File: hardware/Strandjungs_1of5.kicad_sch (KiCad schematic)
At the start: 9 parts, among them J1 Screw_Terminal_01x02, J10 Conn_01x02, J11 Conn_01x02, J12 Conn_01x02, J7 Screw_Terminal_01x02, J8 Screw_Terminal_01x02, J9 Conn_01x02, SW1 SW_DIP_x02

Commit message: first iteration of layout almost done
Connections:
- net RESET: now also A1.9 (D6); no longer A1.8 (D5)
- net TRIGGER: now also A1.8 (D5); no longer A1.9 (D6)
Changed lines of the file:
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@@
     (stroke (width 0) (type default) (color 0 0 0 0))
   )
-  (wire (pts (xy 136.525 83.82) (xy 136.525 94.615))
-    (stroke (width 0) (type default) (color 0 0 0 0))
-  )
-  (wire (pts (xy 136.525 94.615) (xy 151.765 94.615))
+  (wire (pts (xy 137.16 94.615) (xy 151.765 94.615))
     (stroke (width 0) (type default) (color 0 0 0 0))
   )
@@
     (stroke (width 0) (type default) (color 0 0 0 0))
   )
-  (wire (pts (xy 111.76 86.36) (xy 133.985 86.36))
+  (wire (pts (xy 111.76 86.36) (xy 123.825 86.36))
     (stroke (width 0) (type default) (color 0 0 0 0))
   )
@@
   )
   (wire (pts (xy 231.775 34.925) (xy 247.65 34.925))
-    (stroke (width 0) (type default) (color 0 0 0 0))
-  )
-  (wire (pts (xy 133.985 86.36) (xy 133.985 105.41))
     (stroke (width 0) (type default) (color 0 0 0 0))
   )
@@
     (stroke (width 0) (type default) (color 0 0 0 0))
   )
-  (wire (pts (xy 133.985 105.41) (xy 151.765 105.41))
+  (wire (pts (xy 137.16 105.41) (xy 151.765 105.41))
     (stroke (width 0) (type default) (color 0 0 0 0))
   )
@@
     (stroke (width 0) (type default) (color 0 0 0 0))
   )
-  (wire (pts (xy 111.76 83.82) (xy 136.525 83.82))
+  (wire (pts (xy 111.76 83.82) (xy 123.825 83.82))
     (stroke (width 0) (type default) (color 0 0 0 0))
   )
@@
   )
   (label "SWITCH1" (at 233.045 34.925 0)
+    (effects (font (size 1.27 1.27)) (justify left bottom))
+  )
+  (label "TRIGGER" (at 113.0265 83.82 0)
     (effects (font (size 1.27 1.27)) (justify left bottom))
   )
@@
     (effects (font (size 1.27 1.27)) (justify left bottom))
   )
+  (label "RESET" (at 113.03 86.36 0)
+    (effects (font (size 1.27 1.27)) (justify left bottom))
+  )

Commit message: added 7805 as voltage regulator
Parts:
- added R16: dnp, Resistor_SMD:R_0603_1608Metric, symbol Device:R
- added U1: L7805, Package_TO_SOT_THT:TO-220-3_Vertical, symbol Regulator_Linear:L7805
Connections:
- net +12V: now also R16.1, U1.1 (IN)
- net GND: now also U1.2 (GND)
- net +5V: now reaches A1.27 (+5V)
- net +5V: now also U1.3 (OUT)
- net at A1.30 (VIN): now also R16.2
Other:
- note added: "alternative powering if regulator on Arduino supports this"
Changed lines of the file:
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@@
+    (stroke (width 0) (type default) (color 0 0 0 0))
+  )
+  (wire (pts (xy 65.405 53.34) (xy 65.405 54.61))
+    (stroke (width 0) (type default) (color 0 0 0 0))
+  )
+  (wire (pts (xy 101.6 50.8) (xy 101.6 52.07))
     (stroke (width 0) (type default) (color 0 0 0 0))
   )
@@
     (stroke (width 0) (type default) (color 0 0 0 0))
   )
+  (wire (pts (xy 73.025 45.72) (xy 75.565 45.72))
+    (stroke (width 0) (type default) (color 0 0 0 0))
+  )
   (bus (pts (xy 126.365 104.14) (xy 126.365 118.745))
     (stroke (width 0) (type default) (color 0 0 0 0))
@@
     (stroke (width 0) (type default) (color 0 0 0 0))
   )
+  (wire (pts (xy 75.565 45.72) (xy 75.565 43.815))
+    (stroke (width 0) (type default) (color 0 0 0 0))
+  )
   (wire (pts (xy 111.76 76.2) (xy 123.825 76.2))
     (stroke (width 0) (type default) (color 0 0 0 0))
@@
     (stroke (width 0) (type default) (color 0 0 0 0))
   )
+  (wire (pts (xy 93.98 58.42) (xy 93.98 60.96))
+    (stroke (width 0) (type default) (color 0 0 0 0))
+  )
   (bus (pts (xy 229.235 24.765) (xy 229.235 37.465))
     (stroke (width 0) (type default) (color 0 0 0 0))
@@
     (stroke (width 0) (type default) (color 0 0 0 0))
   )
+  (wire (pts (xy 57.785 45.72) (xy 56.515 45.72))
+    (stroke (width 0) (type default) (color 0 0 0 0))
+  )
   (bus (pts (xy 229.235 113.665) (xy 224.155 118.745))
     (stroke (width 0) (type default) (color 0 0 0 0))
@@
     (stroke (width 0) (type default) (color 0 0 0 0))
   )
+  (wire (pts (xy 56.515 44.45) (xy 56.515 45.72))
+    (stroke (width 0) (type default) (color 0 0 0 0))
+  )
   (wire (pts (xy 140.335 78.74) (xy 140.335 80.01))
     (stroke (width 0) (type default) (color 0 0 0 0))
@@
   )
   (bus (pts (xy 126.365 93.98) (xy 126.365 96.52))
+    (stroke (width 0) (type default) (color 0 0 0 0))
+  )
+  (wire (pts (xy 101.6 59.69) (xy 101.6 60.96))
     (stroke (width 0) (type default) (color 0 0 0 0))
   )
@@
     (effects (font (size 1.27 1.27)) (justify left bottom))
   )
+  (text "alternative powering\nif regulator on Arduino\nsupports this"
+    (at 107.95 59.055 0)
+    (effects (font (size 1.27 1.27)) (justify left bottom))
+  )
   (label "SWITCH1" (at 233.045 34.925 0)
     (effects (font (size 1.27 1.27)) (justify left bottom))
@@
   (label "SWITCH3" (at 113.03 96.52 0)
     (effects (font (size 1.27 1.27)) (justify left bottom))
+  )
+  (symbol (lib_id "Regulator_Linear:L7805") (at 65.405 45.72 0) (unit 1)
+    (in_bom yes) (on_board yes) (fields_autoplaced)
+    (property "Reference" "U1" (id 0) (at 65.405 39.8485 0))
+    (property "Value" "L7805" (id 1) (at 65.405 42.6236 0))
+    (property "Footprint" "Package_TO_SOT_THT:TO-220-3_Vertical" (id 2) (at 66.04 49.53 0)
+      (effects (font (size 1.27 1.27) italic) (justify left) hide)
+    )
+    (property "Datasheet" "http://www.st.com/content/ccc/resource/technical/document/datasheet/41/4f/b3/b0/12/d4/47/88/CD00000444.pdf/files/CD00000444.pdf/jcr:content/translations/en.CD00000444.pdf" (id 3) (at 65.405 46.99 0)
+      (effects (font (size 1.27 1.27)) hide)
+    )
+    (pin "1")
+    (pin "2")
+    (pin "3")
   )
   (symbol (lib_id "power:GND") (at 193.04 64.135 0) (mirror y) (unit 1)
@@
     )
     (property "Datasheet" "" (id 3) (at 193.04 64.135 0)
+      (effects (font (size 1.27 1.27)) hide)
+    )
+    (pin "1")
+  )
+  (symbol (lib_id "power:+5V") (at 75.565 43.815 0) (unit 1)
+    (in_bom yes) (on_board yes) (fields_autoplaced)
+    (property "Reference" "#PWR035" (id 0) (at 75.565 47.625 0)
+      (effects (font (size 1.27 1.27)) hide)
+    )
+    (property "Value" "+5V" (id 1) (at 75.565 40.2105 0))
+    (property "Footprint" "" (id 2) (at 75.565 43.815 0)
+      (effects (font (size 1.27 1.27)) hide)
+    )
+    (property "Datasheet" "" (id 3) (at 75.565 43.815 0)
+      (effects (font (size 1.27 1.27)) hide)
+    )
+    (pin "1")
+  )
+  (symbol (lib_id "power:+12V") (at 56.515 44.45 0) (mirror y) (unit 1)
+    (in_bom yes) (on_board yes)
+    (property "Reference" "#PWR033" (id 0) (at 56.515 48.26 0)
+      (effects (font (size 1.27 1.27)) hide)
+    )
+    (property "Value" "+12V" (id 1) (at 56.515 40.8455 0))
+    (property "Footprint" "" (id 2) (at 56.515 44.45 0)
+      (effects (font (size 1.27 1.27)) hide)
+    )
+    (property "Datasheet" "" (id 3) (at 56.515 44.45 0)
+      (effects (font (size 1.27 1.27)) hide)
+    )
+    (pin "1")
+  )
+  (symbol (lib_id "power:GND") (at 65.405 54.61 0) (mirror y) (unit 1)
+    (in_bom yes) (on_board yes) (fields_autoplaced)
+    (property "Reference" "#PWR034" (id 0) (at 65.405 60.96 0)
+      (effects (font (size 1.27 1.27)) hide)
+    )
+    (property "Value" "GND" (id 1) (at 65.405 59.1725 0))
+    (property "Footprint" "" (id 2) (at 65.405 54.61 0)
+      (effects (font (size 1.27 1.27)) hide)
+    )
+    (property "Datasheet" "" (id 3) (at 65.405 54.61 0)
       (effects (font (size 1.27 1.27)) hide)
     )
@@
     (pin "2")
   )
+  (symbol (lib_id "power:+12V") (at 101.6 50.8 0) (mirror y) (unit 1)
+    (in_bom yes) (on_board yes)
+    (property "Reference" "#PWR037" (id 0) (at 101.6 54.61 0)
+      (effects (font (size 1.27 1.27)) hide)
+    )
+    (property "Value" "+12V" (id 1) (at 101.6 47.1955 0))
+    (property "Footprint" "" (id 2) (at 101.6 50.8 0)
+      (effects (font (size 1.27 1.27)) hide)
+    )
+    (property "Datasheet" "" (id 3) (at 101.6 50.8 0)
+      (effects (font (size 1.27 1.27)) hide)
+    )
+    (pin "1")
+  )
   (symbol (lib_id "Connector_Generic:Conn_01x02") (at 199.39 37.465 0) (unit 1)
     (in_bom yes) (on_board yes) (fields_autoplaced)
@@
     (pin "1")
   )
+  (symbol (lib_id "Device:R") (at 101.6 55.88 0) (unit 1)
+    (in_bom yes) (on_board yes) (fields_autoplaced)
+    (property "Reference" "R16" (id 0) (at 103.378 54.9715 0)
+      (effects (font (size 1.27 1.27)) (justify left))
+    )
+    (property "Value" "dnp" (id 1) (at 103.378 57.7466 0)
+      (effects (font (size 1.27 1.27)) (justify left))
+    )
+    (property "Footprint" "Resistor_SMD:R_0603_1608Metric" (id 2) (at 99.822 55.88 90)
+      (effects (font (size 1.27 1.27)) hide)
+    )
+    (property "Datasheet" "~" (id 3) (at 101.6 55.88 0)
+      (effects (font (size 1.27 1.27)) hide)
+    )
+    (pin "1")
+    (pin "2")
+  )
   (symbol (lib_id "Connector_Generic:Conn_01x02") (at 199.39 45.085 0) (unit 1)
     (in_bom yes) (on_board yes) (fields_autoplaced)
@@
     )
     (property "Datasheet" "" (id 3) (at 26.67 19.05 0)
+      (effects (font (size 1.27 1.27)) hide)
+    )
+    (pin "1")
+  )
+  (symbol (lib_id "power:+5V") (at 93.98 58.42 0) (unit 1)
+    (in_bom yes) (on_board yes) (fields_autoplaced)
+    (property "Reference" "#PWR036" (id 0) (at 93.98 62.23 0)
+      (effects (font (size 1.27 1.27)) hide)
+    )
+    (property "Value" "+5V" (id 1) (at 93.98 54.8155 0))
+    (property "Footprint" "" (id 2) (at 93.98 58.42 0)
+      (effects (font (size 1.27 1.27)) hide)
+    )
+    (property "Datasheet" "" (id 3) (at 93.98 58.42 0)
       (effects (font (size 1.27 1.27)) hide)
     )
@@
       (reference "#PWR032") (unit 1) (value "GND") (footprint "")
     )
+    (path "/12938643-23eb-459b-b3a7-66e54527f212"
+      (reference "#PWR033") (unit 1) (value "+12V") (footprint "")
+    )
+    (path "/28aefc84-1f0c-415b-b337-ae32b0353648"
+      (reference "#PWR034") (unit 1) (value "GND") (footprint "")
+    )
+    (path "/118fb43c-3fe2-4064-aed8-f57b6f2acb18"
+      (reference "#PWR035") (unit 1) (value "+5V") (footprint "")
+    )
+    (path "/a6a4eea9-f75e-4f3a-bb3d-08d711b31662"
+      (reference "#PWR036") (unit 1) (value "+5V") (footprint "")
+    )
+    (path "/4944dd57-86a0-4b19-b7ae-1a86b6c1cd4d"
+      (reference "#PWR037") (unit 1) (value "+12V") (footprint "")
+    )
     (path "/fcbd75c3-4fb3-4d23-949d-34c4d3a6ffbc"
       (reference "A1") (unit 1) (value "Arduino_Nano_v2.x") (footprint "Module:Arduino_Nano")
@@
       (reference "R15") (unit 1) (value "5k6") (footprint "Resistor_SMD:R_0603_1608Metric")
     )
+    (path "/943d37e4-3556-46d0-8302-984c6cfecc75"
+      (reference "R16") (unit 1) (value "dnp") (footprint "Resistor_SMD:R_0603_1608Metric")
+    )
     (path "/749d6c0d-beaf-459f-aebf-b9b2a0ea6db2/b6cf11c3-014b-43d0-8df9-33710d313963"
       (reference "R25") (unit 1) (value "56") (footprint "Resistor_SMD:R_0603_1608Metric")
@@
       (reference "SW1") (unit 1) (value "SW_DIP_x02") (footprint "Button_Switch_THT:SW_DIP_SPSTx02_Piano_10.8x6.64mm_W7.62mm_P2.54mm")
     )
-  )
+    (path "/036b33f6-9f67-448b-bbb6-c422f51cb5ec"
+      (reference "U1") (unit 1) (value "L7805") (footprint "Package_TO_SOT_THT:TO-220-3_Vertical")
+    )
+  )

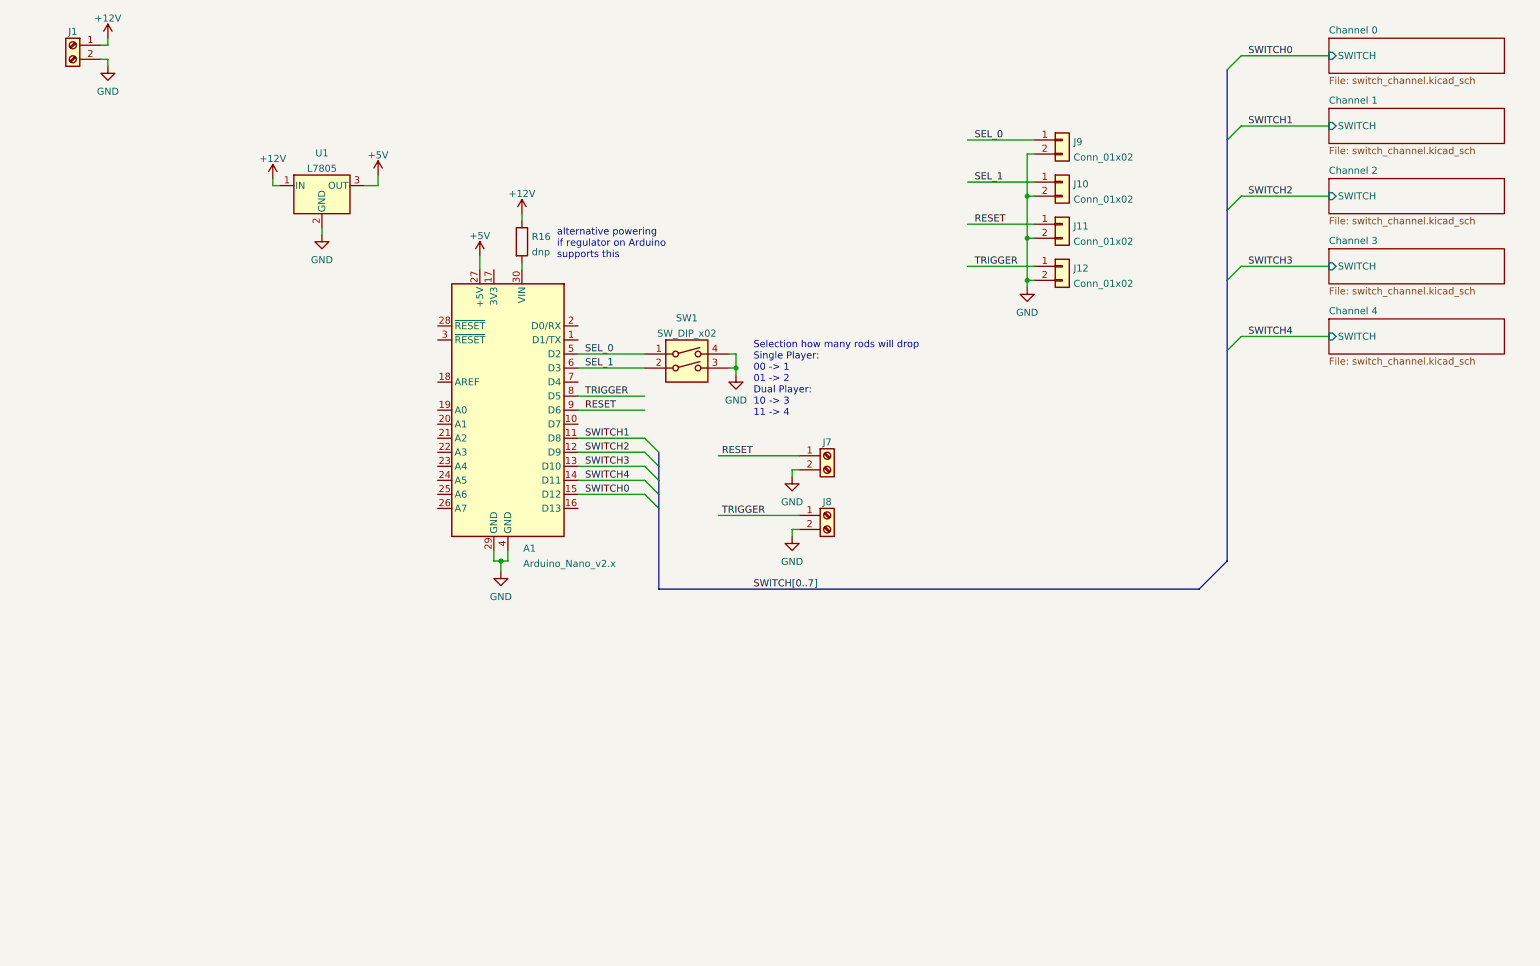
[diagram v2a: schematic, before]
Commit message: updated layout
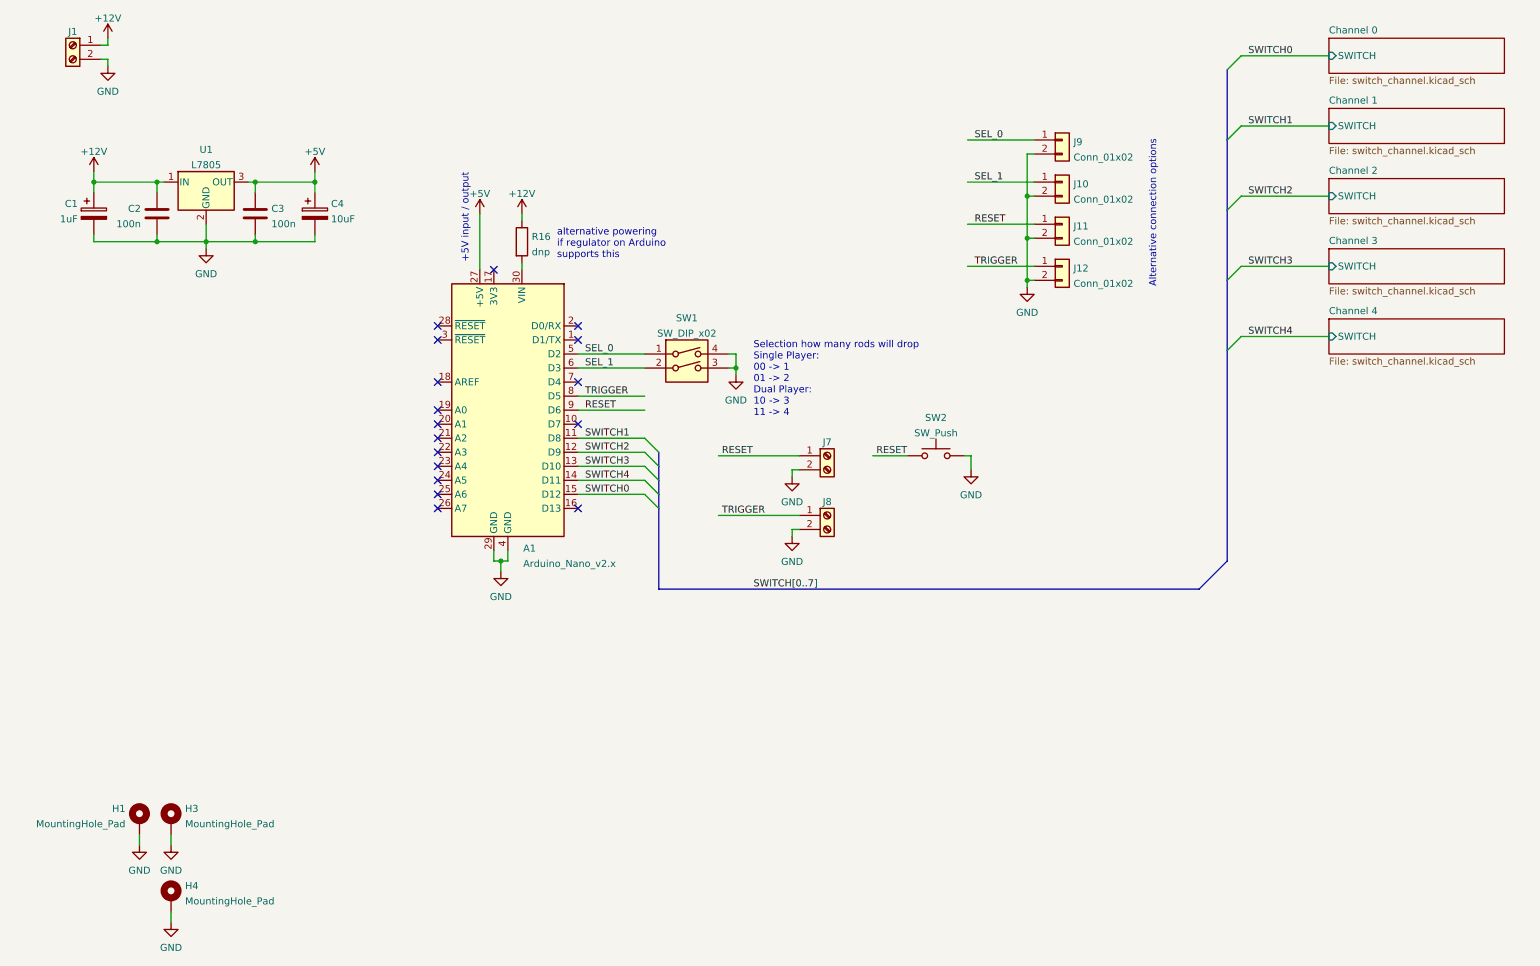
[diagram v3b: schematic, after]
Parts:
- added C1: 1uF, Capacitor_SMD:C_Elec_4x5.4, symbol Device:C_Polarized
- added C2, C3: 100n, Capacitor_SMD:C_0603_1608Metric_Pad1.08x0.95mm_HandSolder, symbol Device:C
- added C4: 10uF, Capacitor_SMD:C_Elec_4x5.4, symbol Device:C_Polarized
- added H1, H3, H4: MountingHole_Pad, MountingHole:MountingHole_3.2mm_M3_Pad_Via, symbol Mechanical:MountingHole_Pad
- added SW2: SW_Push, Button_Switch_THT:SW_Tactile_SKHH_Angled, symbol Switch:SW_Push
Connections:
- net +12V: now also C1.1, C2.1
- net +5V: now also C3.1, C4.1
- net GND: now also C1.2, C2.2, C3.2, C4.2, H1.1, H3.1, H4.1, SW2.2
- net RESET: now also SW2.1
- no-connect marks 0 -> 17
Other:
- note added: "+5V input / output"
- note added: "Alternative connection options"
- moved on the sheet: U1
